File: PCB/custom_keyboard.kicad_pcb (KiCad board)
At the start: 2 copper layers, 385.7 x 135.7 mm, 364 parts, among them IC1 FE2.1, J2 Conn_01x03_Male, Q1 DTC123J, SW1 SW_Push, U1 24LC02BT-I/SN, U10 PRTR5V0U2X, U11 XC6206P332MR, U12 74LVC1G34, U2 PRTR5V0U2X, U4 PRTR5V0U2X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

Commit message: Draft 1-1 with different components
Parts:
- added UD1: Green, LED_SMD:LED_0805_2012Metric, B.Cu at (472.3, 260.3)
- added UD2: Green, LED_SMD:LED_0805_2012Metric, B.Cu at (476.2, 260.3)
- added UD3: Green, LED_SMD:LED_0805_2012Metric, B.Cu at (480.2, 260.3)
- added UD4: Green, LED_SMD:LED_0805_2012Metric, B.Cu at (484.2, 260.3)
- added UD5: Green, LED_SMD:LED_0805_2012Metric, B.Cu at (488.1, 262.7)
- added UD6: Green, LED_SMD:LED_0805_2012Metric, B.Cu at (492.1, 262.7)
- added UD7: Green, LED_SMD:LED_0805_2012Metric, B.Cu at (496.1, 262.7)
- D10: footprint LED_SMD:LED_0402_1005Metric -> LED_SMD:LED_0805_2012Metric
- R16: value 0 -> 470
- R21, R23, R30: footprint Resistor_SMD:R_0805_2012Metric -> Resistor_SMD:R_0603_1608Metric
- U12: footprint Package_TO_SOT_SMD:SOT-353_SC-70-5 -> Package_TO_SOT_SMD:SOT-23-5
- Y2: value 32.768kHZ -> 32.768KHz; footprint Crystal:Crystal_SMD_3225-4Pin_3.2x2.5mm -> Crystal:Crystal_SMD_3215-2Pin_3.2x1.5mm
- moved R38 1.59 mm to (462.7, 261.1)
- moved D10 0.79 mm to (460.3, 261.1)
- moved R1 0.79 mm to (472.3, 262.7)
- moved R17 0.79 mm to (480.2, 262.7)
- moved R18 0.79 mm to (484.2, 262.7)
- moved R7 0.79 mm to (476.2, 262.7)
- moved Y2 0.34 mm to (314.3, 297.3), turned to 90 degrees
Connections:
- Y2 pad 2: GND -> Net-(C9-Pad2)
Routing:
- net GND: track 790.0 -> 770.7 mm
- net HUB_DRV: track 54.5 -> 60.6 mm
- net USB_XTAL1: track 13.9 -> 15.7 mm
- net Net-(C9-Pad2): track 4.12 -> 5.43 mm
- net HUB_LED7: track 40.8 -> 41.6 mm
- net HUB_LED6: track 36.7 -> 37.5 mm
- net HUB_LED4: track 48.7 -> 47.9 mm
- net HUB_LED3: track 36.5 -> 35.7 mm
- net HUB_LED2: track 31.5 -> 30.7 mm
- net HUB_LED1: track 29.0 -> 28.3 mm
- net Net-(R29-Pad1): track 1.76 -> 2.39 mm
- net Net-(R26-Pad1): track 1.76 -> 2.39 mm
- net Net-(D10-Pad1): track 1.76 -> 2.39 mm
- net Net-(R7-Pad1): track 1.76 -> 2.39 mm
- net Net-(R1-Pad1): track 1.76 -> 2.39 mm
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
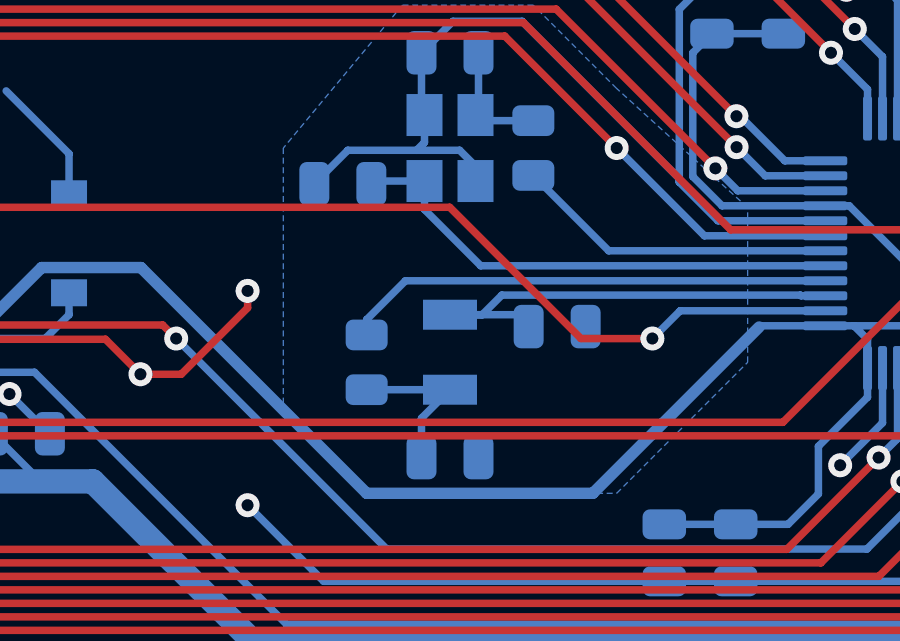
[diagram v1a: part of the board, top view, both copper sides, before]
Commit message: Routed GND to crystal
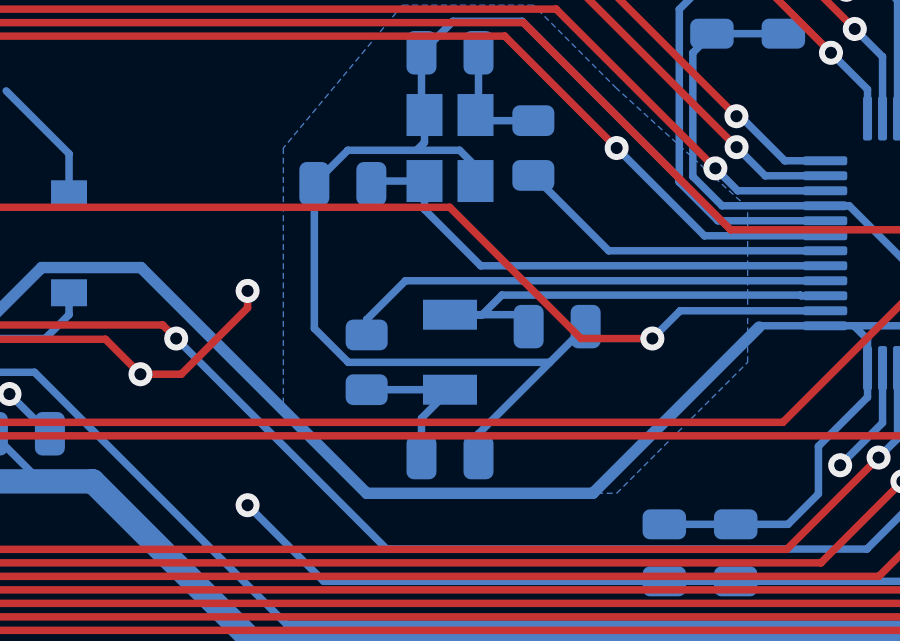
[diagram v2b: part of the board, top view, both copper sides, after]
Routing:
- net GND: track 770.7 -> 789.7 mm
